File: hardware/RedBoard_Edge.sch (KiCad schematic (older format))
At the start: 72 parts, among them J1 CONN_025MM, J17 QWIIC_CONNECTORJS-1MM, J2 CONN_03X2SMT, J20 POWER_JACKSMD, J4 USB_MICRO-B_FEMALE-SMT, J5 CONN_04, J6 CONN_04, Q1 MOSFET_PCH-SI2309DS, Q2 MOSFET-NCH-BSS138, Q3 MOSFET-NCH-BSS138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

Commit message: Post double check changes
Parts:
- removed D5: SPARKFUN-LED_LED-YELLOW-550, LED:LED_550_T1-.75_RT_ANG_PCB, symbol SPARKFUN-LED_LED-YELLOW-550
- added D5: LED-BLUE, LED:LED_550_T1-.75_RT_ANG_PCB, symbol SPARKFUN-LED_LED-BLUE-550
- C1, C12, C2, C4, C8: value 0.1UF-0603-25V-_+80_-20%_ -> 0.1UF
- C10, C9: value 10PF-0603-50V-5% -> 10PF
- C11: value 10NF-0603-50V-10% -> 10NF
- C3, C6: value 10UF-POLAR-EIA3216-16V-10%_TANT_ -> 10UF-TANT
- C5: value 47UF-POLAR-PANASONIC_D-35V-20% -> 47UF-35V
- C7: value 1.0UF-0603-16V-10% -> 1.0UF
- D1: value DIODE-SHOTTKY_MBRA140 -> SHOTTKY_MBRA140
- D2: value SPARKFUN-LED_LED-YELLOW-550 -> LED-YELLOW
- D3: value SPARKFUN-LED_LED-GREEN-550 -> LED-GREEN
- D4: value SPARKFUN-LED_LED-RED-550 -> LED-RED
- J4: value USB_MICRO-B_FEMALE-SMT -> USB_MICRO-B
- JP1, JP2: value JUMPER-SMT_2_NO -> JUMPER
- Q1: value MOSFET_PCH-SI2309DS -> MOSFET-SI2309DS
- Q2, Q3: value MOSFET-NCH-BSS138 -> BSS138
- R1, R2, R5, R6: value 470OHM-0603-1_10W-1% -> 470OHM
- R10, R7, R8, R9: value 4.7KOHM-0603-1_10W-1% -> 4.7KOHM
- R14: value 715OHM-0603-1_10W-1% -> 715OHM
- R15: value 240OHM-0603-1_10W-1% -> 240OHM
- R3, R4: value 10KOHM-0603-1_10W-1% -> 10KOHM
- S1: value MOMENTARY-SWITCH-SPST-2-PTH-RT-ANGLE -> MOMENTARY-SWITCH
- S2: value SWITCH_TOGGLE_SPST_RIGHT_ANGLE -> SWITCH_TOGGLE
- U2: value V_REG_MIC52053.3V -> MIC5205-3.3V
- U4: value ATMEGA328P_TQFP -> ATMEGA328
- U6: value V_REG_LM1117SOT223 -> LM1117
- Y1: value RESONATOR-16MHZSMD_3.2X1.3 -> RESONATOR-16MHZ
- Y2: value CRYSTAL-12MHZ\" -> CRYSTAL-12MHZ
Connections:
- net GND: now also D5.1 (C)
- net at R1.2: now also D5.2 (A)
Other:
- note added: "The Standoffs on the left side\nof the board can be connected\nto the grounds for the USB shield\nor the board ground by connecting\ntheir repsective jumpers."
- note removed: "The Standoffs on the left side"
- note removed: "of the board can be connected"
- note removed: "or the board ground by connecting"
- note removed: "their respective jumpers."
- note removed: "to the grounds for the USB shield"
- moved on the sheet: J20, S2, U3, U5

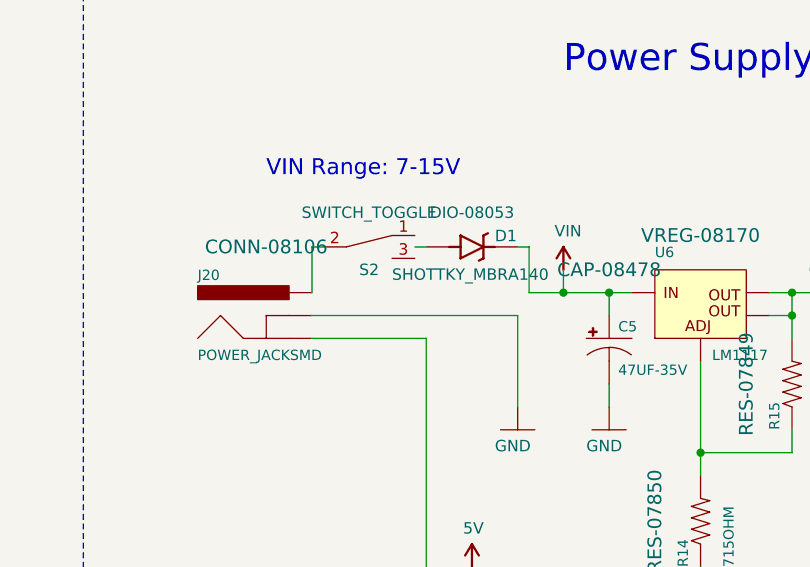
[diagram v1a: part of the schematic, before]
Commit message: updated toggle switch
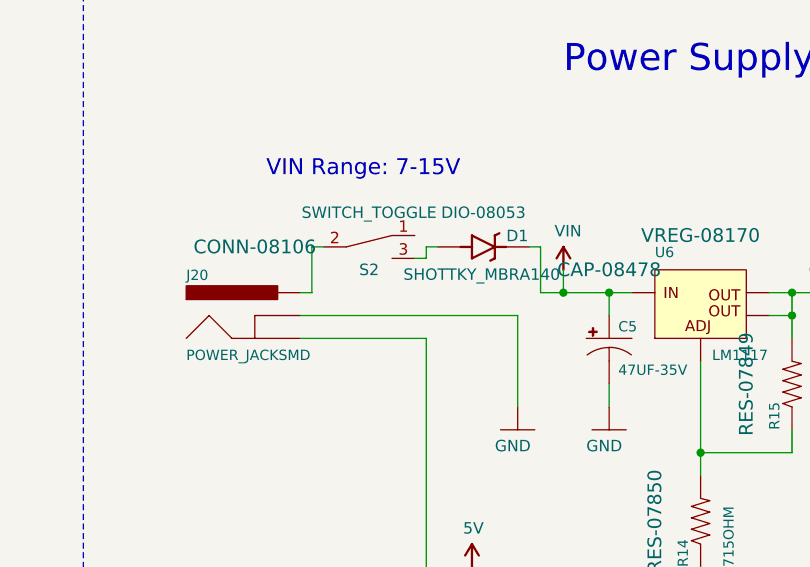
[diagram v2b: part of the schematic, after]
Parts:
- S2: footprint (none) -> Switches:TOGGLE_SWITCH-102-C3
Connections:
- net at D1.A: now also S2.3
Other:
- moved on the sheet: D1, J20
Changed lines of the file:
@@
 L POWER_JACKSMD J20
 U 1 1 59EFD228
-P 6650 1900
-F 0 "J20" H 6350 2050 45  0000 L BNN
-F 1 "POWER_JACKSMD" H 6350 1700 45  0000 L BNN
-F 2 "Connectors:POWER_JACK_SMD_GND" H 6650 2150 20  0001 C CNN
-F 3 "" H 6650 1900 50  0001 C CNN
-F 4 "CONN-08106" H 6650 2200 60  0000 C CNN "Field4"
-	1    6650 1900
+P 6600 1900
+F 0 "J20" H 6300 2050 45  0000 L BNN
+F 1 "POWER_JACKSMD" H 6300 1700 45  0000 L BNN
+F 2 "Connectors:POWER_JACK_SMD_GND" H 6600 2150 20  0001 C CNN
+F 3 "" H 6600 1900 50  0001 C CNN
+F 4 "CONN-08106" H 6600 2200 60  0000 C CNN "Field4"
+	1    6600 1900
 	1    0    0    -1
 $EndComp
@@
 L DIODE-SHOTTKY_MBRA140 D1
 U 1 1 59F0F4F3
-P 7550 1600
-F 0 "D1" H 7650 1619 50  0000 L BNN
-F 1 "SHOTTKY_MBRA140" H 7200 1450 50  0000 L BNN
-F 2 "Silicon-Standard:SMA-DIODE" H 8200 1450 50  0001 C CNN
-F 3 "" H 7550 1600 50  0001 C CNN
-F 4 "DIO-08053" H 7550 1750 50  0000 C CNN "Field4"
-	1    7550 1600
+P 7600 1600
+F 0 "D1" H 7700 1619 50  0000 L BNN
+F 1 "SHOTTKY_MBRA140" H 7250 1450 50  0000 L BNN
+F 2 "Silicon-Standard:SMA-DIODE" H 8250 1450 50  0001 C CNN
+F 3 "" H 7600 1600 50  0001 C CNN
+F 4 "DIO-08053" H 7600 1750 50  0000 C CNN "Field4"
+	1    7600 1600
 	1    0    0    -1
 $EndComp
@@
 Connection ~ 12900 4500
 Wire Wire Line
-	6850 1900 7750 1900
+	6800 1900 7750 1900
 Wire Wire Line
 	7750 1900 7750 2300
@@
 	9950 4600 9950 4400
 Wire Wire Line
-	6850 2000 7350 2000
+	6800 2000 7350 2000
 Wire Wire Line
 	7350 2000 7350 3700
@@
 	6550 7100 6550 7000
 Wire Wire Line
-	7800 1800 8250 1800
-Wire Wire Line
-	7800 1800 7800 1600
-Wire Wire Line
-	7800 1600 7750 1600
-Wire Wire Line
-	7300 1600 7350 1600
+	7850 1800 8250 1800
+Wire Wire Line
+	7850 1800 7850 1600
+Wire Wire Line
+	7850 1600 7800 1600
 Wire Wire Line
 	2300 2900 2300 2450
@@
 F 0 "S2" H 7100 1500 50  0000 C CNN
 F 1 "SWITCH_TOGGLE" H 7100 1750 50  0000 C CNN
-F 2 "" H 7100 1600 50  0001 C CNN
+F 2 "Switches:TOGGLE_SWITCH-102-C3" H 7100 1600 50  0001 C CNN
 F 3 "" H 7100 1600 50  0001 C CNN
 F 4 "PRT-13888" H 7100 1400 50  0001 C CNN "Field4"
@@
 	0    1    1    0
 $EndComp
+Wire Wire Line
+	6850 1800 6800 1800
+Wire Wire Line
+	7350 1650 7300 1650
+Wire Wire Line
+	7350 1650 7350 1600
+Wire Wire Line
+	7350 1600 7400 1600
 $EndSCHEMATC

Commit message: fixed xtal
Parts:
- Y2: footprint Clocks:CRYSTAL-SMD-5X3.2-4PAD -> Clocks:CRYSTAL-SMD-3.2X2.5MM
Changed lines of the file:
@@
 F 0 "Y2" V 3000 2850 45  0000 L BNN
 F 1 "CRYSTAL-12MHZ" V 3100 2600 45  0000 L BNN
-F 2 "Clocks:CRYSTAL-SMD-5X3.2-4PAD" H 2980 3150 20  0001 C CNN
+F 2 "Clocks:CRYSTAL-SMD-3.2X2.5MM" H 2980 3150 20  0001 C CNN
 F 3 "" H 2950 3000 50  0001 C CNN
 F 4 "XTAL-13518" H 3110 3215 60  0000 C CNN "Field4"

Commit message: checklist changes
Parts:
- removed J2: CONN_03X2SMT, Connectors:2X3-NS, symbol CONN_03X2SMT
- added J2: CONN_03X22X3_SILK_MALE_PTH, 2X3, symbol CONN_03X22X3_SILK_MALE_PTH
- S1: value MOMENTARY-SWITCH -> MOMENTARY-SWITCH-SPST-2-PTH-RT-ANGLE; footprint Switches:SWITCH TACTILE SPST-NO 0.05A 12V -> Switches:TACTILE_SWITCH_PTH_RIGHT_ANGLE_KIT; Field4 CONN-10672 -> CONN-13896
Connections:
- net 5V: now also J2.2
- net GND: now also J2.6
- net MISO: now also J2.1
- net MOSI: now also J2.4
- net RESET: now also J2.5
- net SCK: now also J2.3
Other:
- note added: "v10"
- note removed: "v02"
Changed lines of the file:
@@
-$EndComp
-$Comp
-L CONN_03X2SMT J2
-U 1 1 59F12EC0
-P 2850 4550
-F 0 "J2" H 2700 4750 45  0000 L BNN
-F 1 "CONN_03X2SMT" H 2700 4300 45  0000 L BNN
-F 2 "Connectors:2X3-NS" H 2850 4850 20  0001 C CNN
-F 3 "" H 2850 4550 50  0001 C CNN
-F 4 "CONN-11415" H 2850 4900 60  0000 C CNN "Field4"
-	1    2850 4550
-	1    0    0    -1
 $EndComp
 $Comp
@@
 $EndComp
 $Comp
-L MOMENTARY-SWITCH-SPST-2-PTH-RT-ANGLE S1
-U 1 1 59F24A23
-P 11900 2300
-F 0 "S1" H 11700 2350 45  0000 L BNN
-F 1 "MOMENTARY-SWITCH" H 11700 2100 45  0000 L BNN
-F 2 "Switches:SWITCH TACTILE SPST-NO 0.05A 12V" H 11600 2250 50  0001 C CNN
-F 3 "" H 11900 2300 50  0001 C CNN
-F 4 "CONN-10672" H 11900 2550 50  0000 C CNN "Field4"
-	1    11900 2300
-	1    0    0    -1
-$EndComp
-$Comp
 L CH340GSMD U1
 U 1 1 59F21E1E
@@
 Revised by: Andy England
 Text Notes 15950 10350 0    50   ~ 0
-v02
+v10
 Text Notes 6250 6350 0    50   ~ 0
 The Standoffs on the left side\nof the board can be connected\nto the grounds for the USB shield\nor the board ground by connecting\ntheir repsective jumpers.
@@
 Wire Wire Line
 	7350 1600 7400 1600
+$Comp
+L CONN_03X22X3_SILK_MALE_PTH J2
+U 1 1 5A7CB194
+P 2850 4550
+F 0 "J2" H 2700 4750 45  0000 L BNN
+F 1 "CONN_03X22X3_SILK_MALE_PTH" H 2700 4300 45  0000 L BNN
+F 2 "2X3" H 2850 4850 20  0001 C CNN
+F 3 "" H 2850 4550 50  0001 C CNN
+F 4 "CONN-09701" H 2850 4900 60  0000 C CNN "Field4"
+	1    2850 4550
+	1    0    0    -1
+$EndComp
+$Comp
+L MOMENTARY-SWITCH-SPST-2-PTH-RT-ANGLE S1
+U 1 1 5A7CC30D
+P 11900 2300
+F 0 "S1" H 11700 2350 45  0000 L BNN
+F 1 "MOMENTARY-SWITCH-SPST-2-PTH-RT-ANGLE" H 11700 2100 45  0000 L BNN
+F 2 "Switches:TACTILE_SWITCH_PTH_RIGHT_ANGLE_KIT" H 11600 2250 50  0001 C CNN
+F 3 "" H 11900 2300 50  0001 C CNN
+F 4 "CONN-13896" H 11900 2550 50  0000 C CNN "Field4"
+	1    11900 2300
+	1    0    0    -1
+$EndComp
 $EndSCHEMATC

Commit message: QC Checklist changes
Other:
- moved on the sheet: C10, Y2
